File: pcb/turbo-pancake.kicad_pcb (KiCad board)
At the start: 2 copper layers, 22 parts, among them J1 Conn_01x04, J2 Conn_01x12, J3 Conn_01x12, SW1 MX_LED, SW2 MX_LED, SW3 MX_LED, SW4 MX_LED, SW5 MX_LED, SW6 MX_LED, SW7 MX_LED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

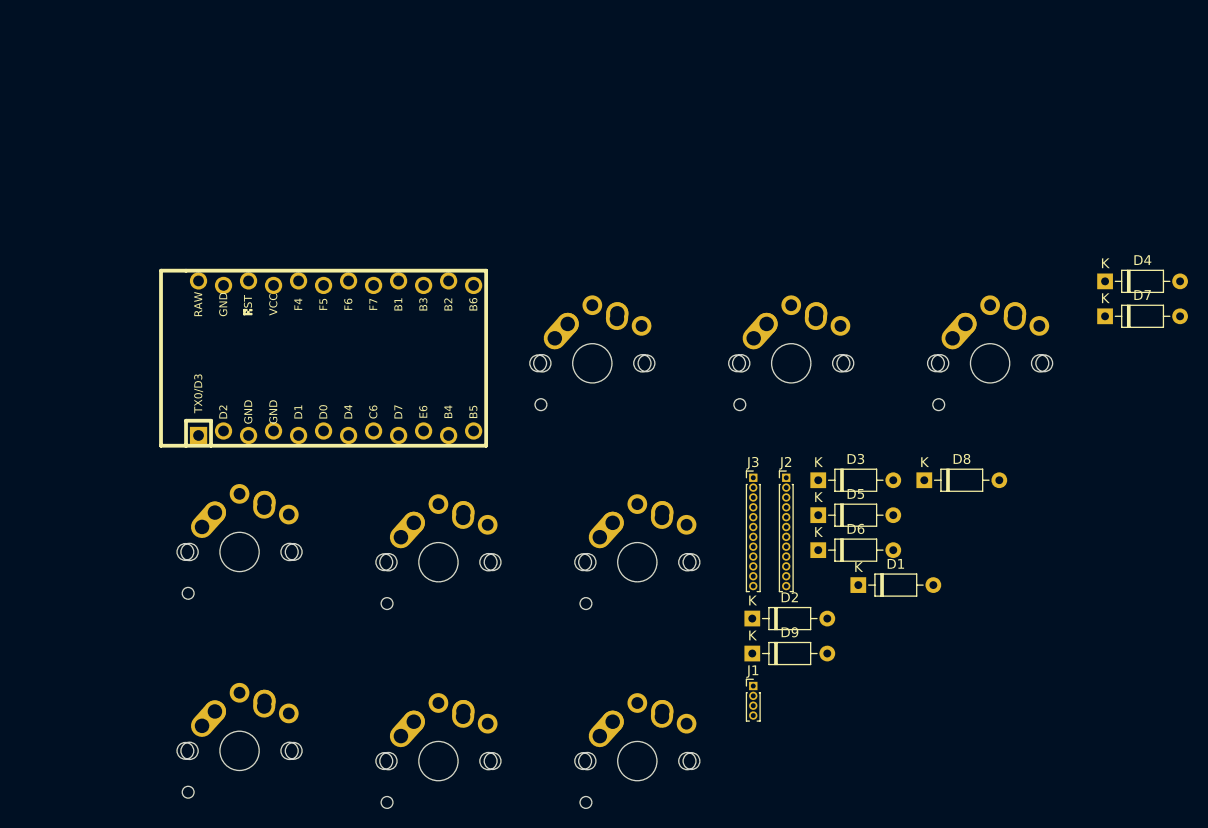
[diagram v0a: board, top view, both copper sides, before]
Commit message: pcb parts placed
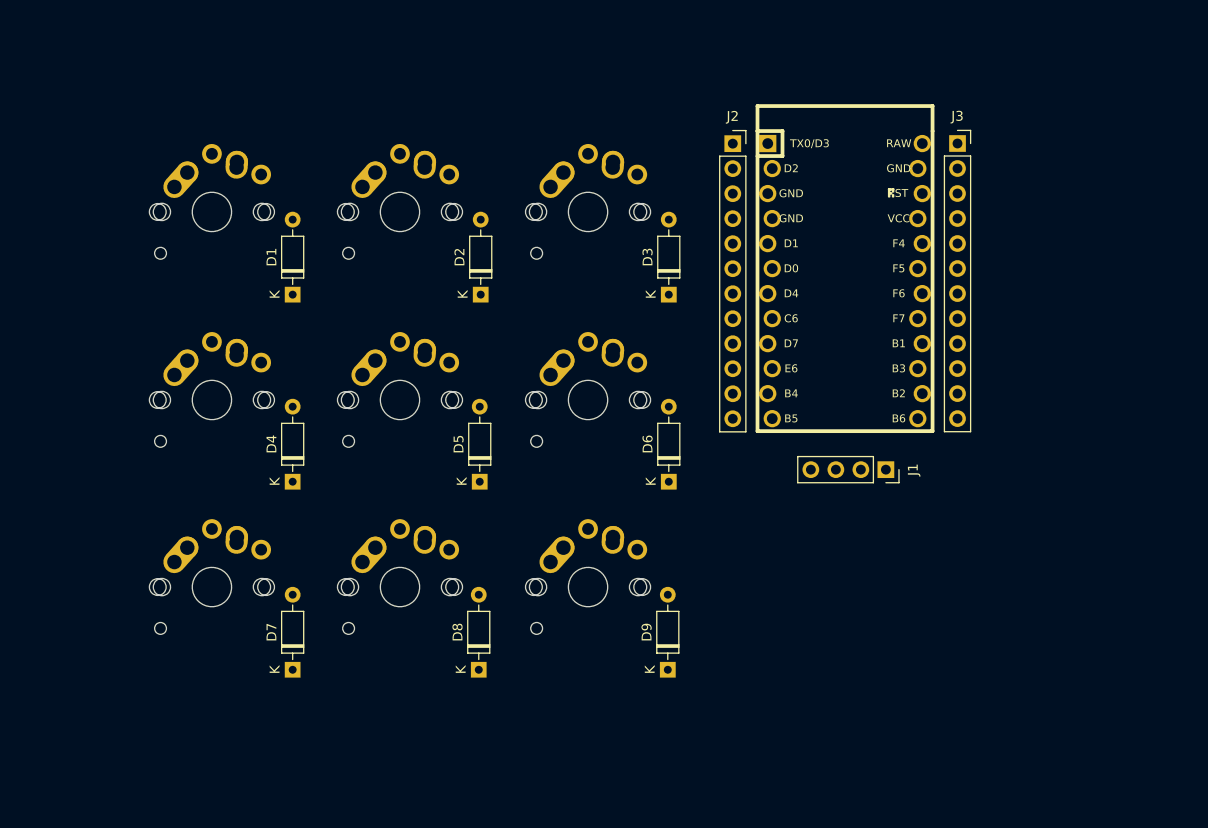
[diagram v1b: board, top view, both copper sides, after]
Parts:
- J1: footprint Connector_PinHeader_1.00mm:PinHeader_1x04_P1.00mm_Vertical -> Connector_PinSocket_2.54mm:PinSocket_1x04_P2.54mm_Vertical
- J2, J3: footprint Connector_PinHeader_1.00mm:PinHeader_1x12_P1.00mm_Vertical -> Connector_PinSocket_2.54mm:PinSocket_1x12_P2.54mm_Vertical
- moved D7 90.0 mm to (107.7, 96.0), turned to 90 degrees
- moved D4 85.0 mm to (107.7, 76.9), turned to 90 degrees
- moved D1 64.6 mm to (107.7, 57.9), turned to 90 degrees
- moved SW8 64.1 mm to (118.6, 87.6)
- moved SW2 57.1 mm to (118.6, 49.5)
- moved U1 52.3 mm to (163.8, 56.5), turned to 270 degrees
- moved SW3 49.5 mm to (137.7, 49.5)
- moved D8 49.2 mm to (126.6, 96.0), turned to 90 degrees
- moved SW7 43.3 mm to (99.5, 87.6)
- moved D2 42.9 mm to (126.8, 57.9), turned to 90 degrees
- moved SW1 41.6 mm to (99.5, 49.5)
- moved SW5 39.9 mm to (118.6, 68.6)
- moved J3 39.8 mm to (175.2, 42.5)
- moved SW6 39.7 mm to (137.7, 68.6)
- moved D5 34.5 mm to (126.7, 76.9), turned to 90 degrees
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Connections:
- J1 pad 2: VCC -> RAW

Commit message: creating space
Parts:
- moved J1 20.4 mm to (188.3, 77.2)
- moved J2 20.4 mm to (172.8, 44.1)
- moved J3 20.4 mm to (195.6, 44.0)
- moved U1 20.4 mm to (184.2, 58.0)
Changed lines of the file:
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@@
   )
   (module Connector_PinSocket_2.54mm:PinSocket_1x12_P2.54mm_Vertical (layer F.Cu)
-    (at 175.225 42.55)
+    (at 195.575 44.05)
     (descr "Through hole straight socket strip, 1x12, 2.54mm pitch, single row (from Kicad 4.0.7), script generated")
     (tags "Through hole socket strip THT 1x12 2.54mm single row")
@@
   )
   (module Connector_PinSocket_2.54mm:PinSocket_1x12_P2.54mm_Vertical (layer F.Cu)
-    (at 152.4 42.565)
+    (at 172.75 44.065)
     (descr "Through hole straight socket strip, 1x12, 2.54mm pitch, single row (from Kicad 4.0.7), script generated")
     (tags "Through hole socket strip THT 1x12 2.54mm single row")
@@
   )
   (module Connector_PinSocket_2.54mm:PinSocket_1x04_P2.54mm_Vertical (layer F.Cu)
-    (at 167.95 75.675 270)
+    (at 188.3 77.175 270)
     (descr "Through hole straight socket strip, 1x04, 2.54mm pitch, single row (from Kicad 4.0.7), script generated")
     (tags "Through hole socket strip THT 1x04 2.54mm single row")
@@
   )
   (module Keebio-Parts:ArduinoProMicro-ZigZag (layer F.Cu)
-    (at 163.8 56.525 270)
+    (at 184.15 58.025 270)
     (fp_text reference U1 (at 0 1.625 90) (layer F.SilkS) hide
       (effects (font (size 1 1) (thickness 0.2)))

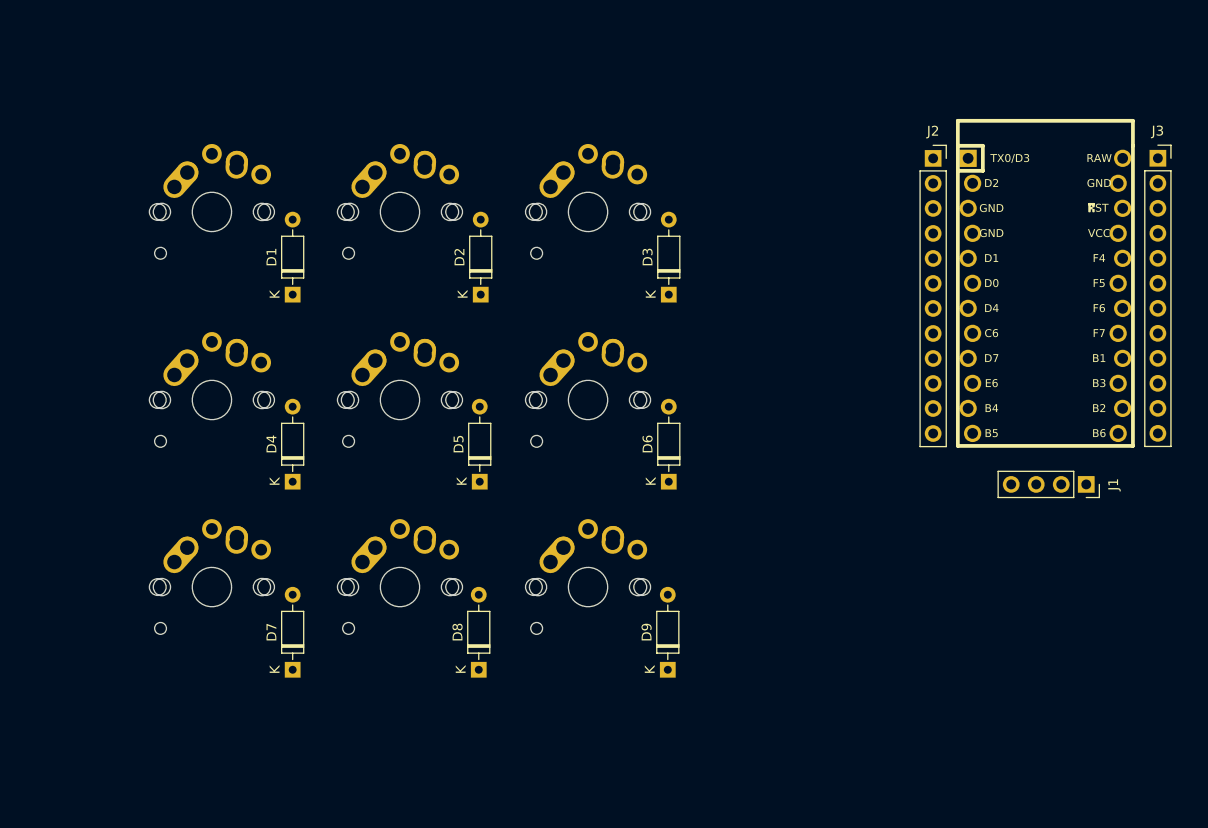
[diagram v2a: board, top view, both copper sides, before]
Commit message: wired up power traces are too small
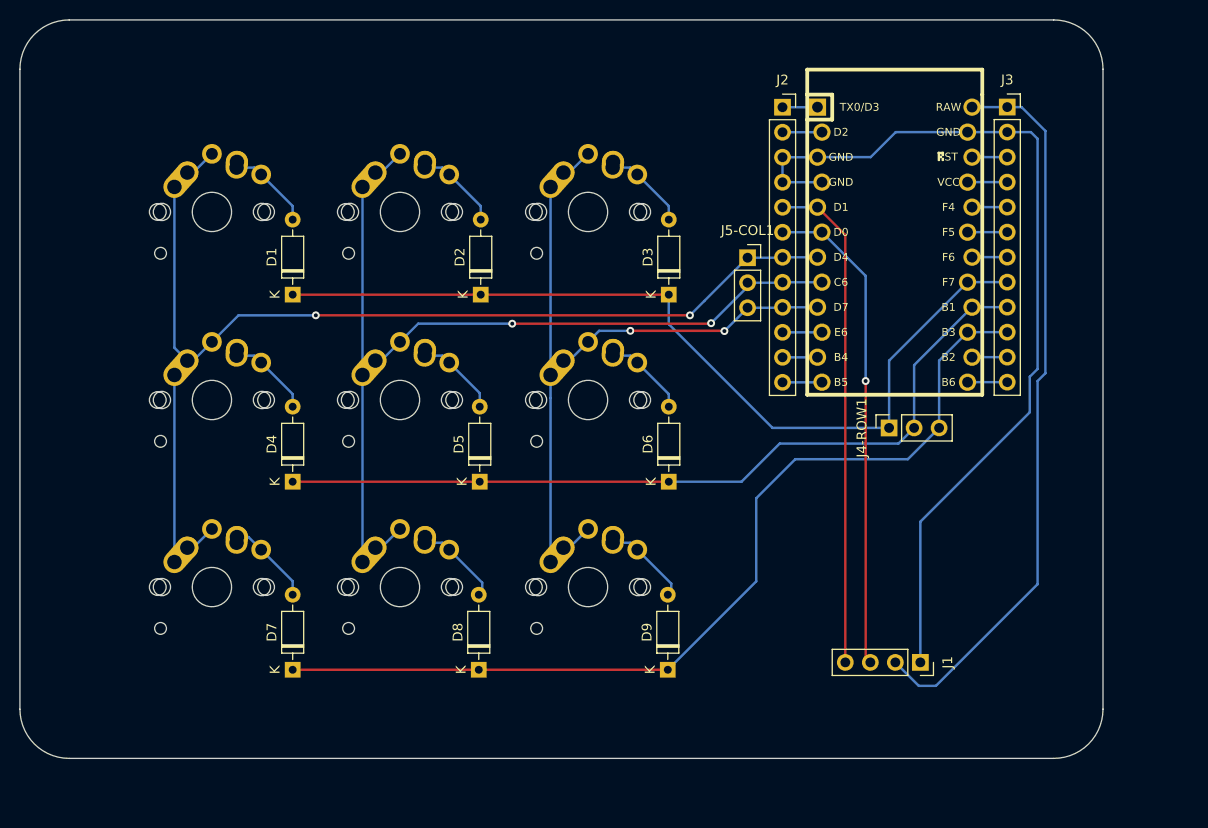
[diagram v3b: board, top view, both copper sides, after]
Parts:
- added J4-ROW1: Conn_01x03, Connector_PinSocket_2.54mm:PinSocket_1x03_P2.54mm_Vertical, F.Cu at (168.3, 71.4)
- added J5-COL1: Conn_01x03, Connector_PinSocket_2.54mm:PinSocket_1x03_P2.54mm_Vertical, F.Cu at (153.9, 54.1)
- moved J1 24.7 mm to (171.4, 95.2)
- moved J2 16.2 mm to (157.4, 38.9)
- moved U1 16.2 mm to (168.8, 52.8)
- moved J3 16.2 mm to (180.3, 38.9)
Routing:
- net A6-D4-PD4: track 0.00 -> 118.1 mm, vias 0 -> 2
- net COL1: track 0.00 -> 97.6 mm, vias 0 -> 2
- net D14-PB3-MISO: track 0.00 -> 95.7 mm
- net GND: track 0.00 -> 91.9 mm
- net A0-PF7-D18: track 0.00 -> 90.1 mm
- net D15-PB1-SCLK: track 0.00 -> 83.7 mm
- net A7-D6-PD7: track 0.00 -> 76.8 mm, vias 0 -> 2
- net RAW: track 0.00 -> 74.5 mm
- net D2-PD1-SDA: track 0.00 -> 51.0 mm
- net D3-PD0-SCL: track 0.00 -> 49.7 mm, vias 0 -> 1
- net Net-(D9-Pad2): track 0.00 -> 8.94 mm
- net Net-(D8-Pad2): track 0.00 -> 8.90 mm
- net Net-(D7-Pad2): track 0.00 -> 8.90 mm
- net Net-(D3-Pad2): track 0.00 -> 8.70 mm
- net Net-(D2-Pad2): track 0.00 -> 8.70 mm
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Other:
- board outline added: 110 x 75 mm

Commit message: rewired
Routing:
- net RAW: track 74.5 -> 68.7 mm
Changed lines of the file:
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@@
     (thickness 1.6)
     (drawings 352)
-    (tracks 205)
+    (tracks 203)
     (zones 0)
     (modules 24)
@@
     (38 B.Mask user)
     (39 F.Mask user)
-    (40 Dwgs.User user hide)
+    (40 Dwgs.User user)
     (41 Cmts.User user)
     (42 Eco1.User user)
@@
   (segment (start 176.7036 38.85) (end 176.6986 38.855) (width 0.25) (layer B.Cu) (net 31))
   (segment (start 180.275 38.85) (end 176.7036 38.85) (width 0.25) (layer B.Cu) (net 31))
-  (segment (start 171.29125 97.63125) (end 168.91 95.25) (width 0.25) (layer B.Cu) (net 31))
-  (segment (start 173.0375 97.63125) (end 171.29125 97.63125) (width 0.25) (layer B.Cu) (net 31))
-  (segment (start 181.725 38.85) (end 184.15 41.275) (width 0.25) (layer B.Cu) (net 31))
-  (segment (start 184.15 41.275) (end 184.15 65.88125) (width 0.25) (layer B.Cu) (net 31))
-  (segment (start 180.275 38.85) (end 181.725 38.85) (width 0.25) (layer B.Cu) (net 31))
-  (segment (start 184.15 65.88125) (end 183.35625 66.675) (width 0.25) (layer B.Cu) (net 31))
-  (segment (start 183.35625 66.675) (end 183.35625 87.3125) (width 0.25) (layer B.Cu) (net 31))
-  (segment (start 183.35625 87.3125) (end 173.0375 97.63125) (width 0.25) (layer B.Cu) (net 31))
+  (segment (start 168.91 86.6775) (end 183.35625 72.23125) (width 0.25) (layer F.Cu) (net 31))
+  (segment (start 168.91 95.25) (end 168.91 86.6775) (width 0.25) (layer F.Cu) (net 31))
+  (segment (start 180.275 38.85) (end 181.725 38.85) (width 0.25) (layer F.Cu) (net 31))
+  (segment (start 181.725 38.85) (end 184.15 41.275) (width 0.25) (layer F.Cu) (net 31))
+  (segment (start 184.15 71.4375) (end 183.35625 72.23125) (width 0.25) (layer F.Cu) (net 31))
+  (segment (start 184.15 41.275) (end 184.15 71.4375) (width 0.25) (layer F.Cu) (net 31))
 )
